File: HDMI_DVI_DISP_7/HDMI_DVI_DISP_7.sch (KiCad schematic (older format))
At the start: 0 parts

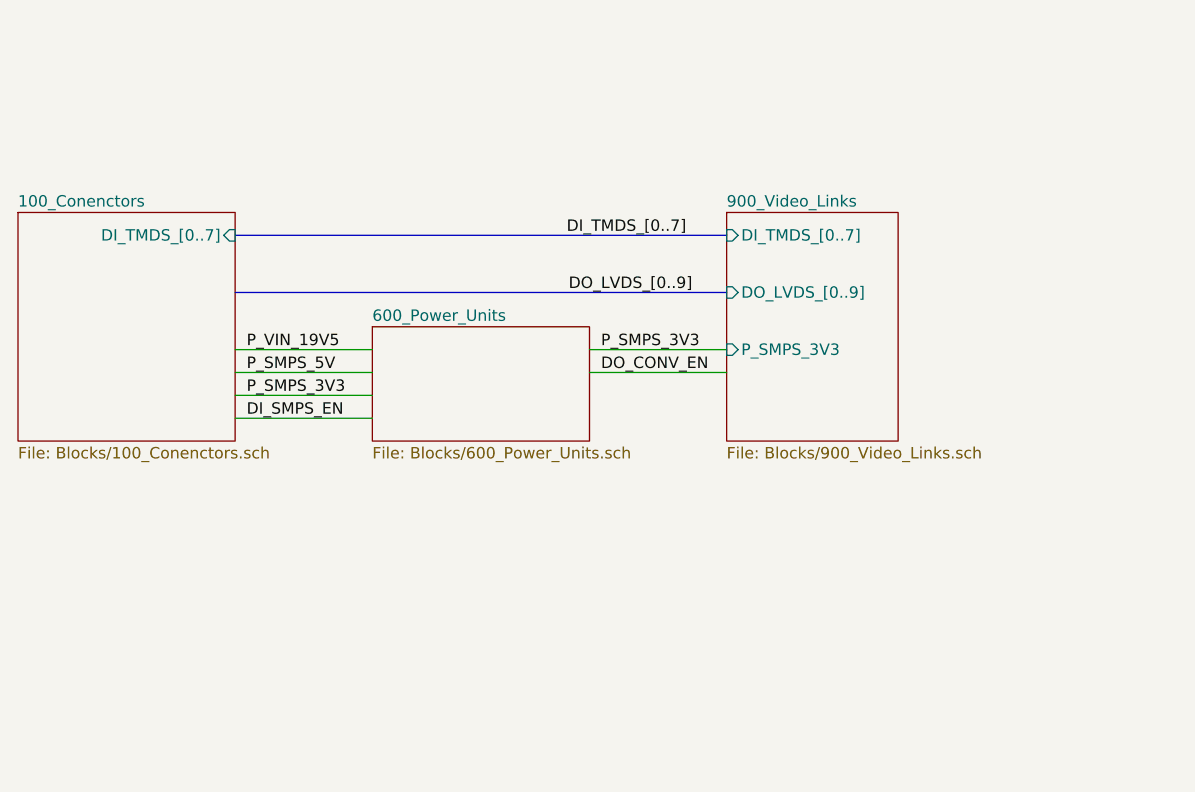
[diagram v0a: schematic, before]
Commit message: The base structure defined for PS
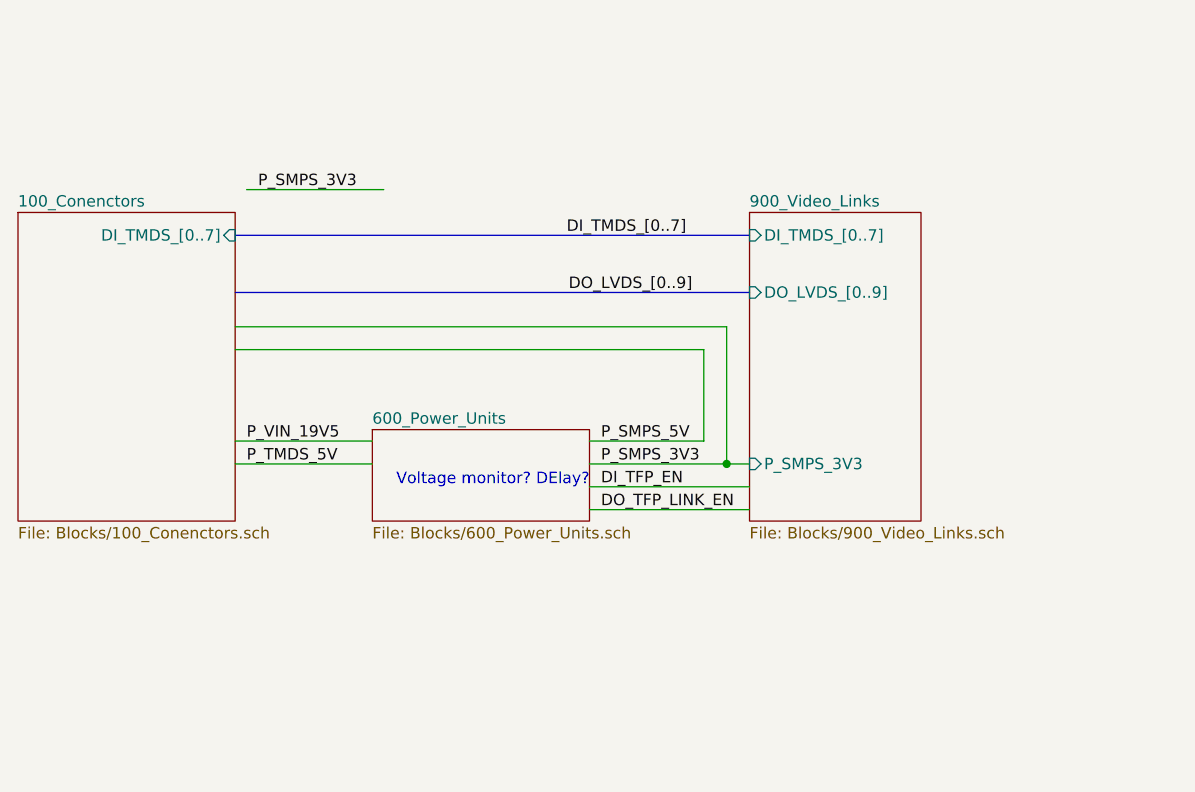
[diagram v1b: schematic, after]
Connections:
- net labels added: DI_TFP_EN, DO_TFP_LINK_EN, P_TMDS_5V
- net labels removed: DI_SMPS_EN, DO_CONV_EN
- wire segments 6 -> 12
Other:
- note added: "Voltage monitor? DElay?"
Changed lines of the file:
@@
 $EndDescr
 $Sheet
-S 3850 2900 950  1000
+S 3850 2900 950  1350
 U 607739A5
 F0 "100_Conenctors" 50
@@
 $EndSheet
 $Sheet
-S 5400 3400 950  500
+S 5400 3850 950  400
 U 60773A19
 F0 "600_Power_Units" 50
@@
 $EndSheet
 $Sheet
-S 6950 2900 750  1000
+S 7050 2900 750  1350
 U 60773BC4
 F0 "900_Video_Links" 50
 F1 "Blocks/900_Video_Links.sch" 50
-F2 "DO_LVDS_[0..9]" I L 6950 3250 50
-F3 "DI_TMDS_[0..7]" I L 6950 3000 50
-F4 "P_SMPS_3V3" I L 6950 3500 50
+F2 "DO_LVDS_[0..9]" I L 7050 3250 50
+F3 "DI_TMDS_[0..7]" I L 7050 3000 50
+F4 "P_SMPS_3V3" I L 7050 4000 50
 $EndSheet
 Text Label 6800 3250 2    50   ~ 0
 DO_LVDS_[0..9]
 Wire Bus Line
-	6950 3000 4800 3000
+	7050 3000 4800 3000
 Text Label 6250 3000 0    50   ~ 0
 DI_TMDS_[0..7]
 Wire Bus Line
-	6950 3250 4800 3250
+	7050 3250 4800 3250
 Wire Wire Line
-	6350 3500 6950 3500
-Text Label 6400 3500 0    50   ~ 0
+	6350 4000 6950 4000
+Text Label 6400 4000 0    50   ~ 0
 P_SMPS_3V3
-Text Label 4850 3500 0    50   ~ 0
+Text Label 4850 3900 0    50   ~ 0
 P_VIN_19V5
 Wire Wire Line
-	4800 3500 5400 3500
-Wire Wire Line
-	4800 3600 5400 3600
-Text Label 4850 3600 0    50   ~ 0
+	4800 3900 5400 3900
+Text Label 6400 3900 0    50   ~ 0
 P_SMPS_5V
-Text Label 4850 3700 0    50   ~ 0
+Text Label 4900 2800 0    50   ~ 0
 P_SMPS_3V3
 Wire Wire Line
-	4800 3700 5400 3700
+	4850 2800 5450 2800
 Wire Wire Line
-	4800 3800 5400 3800
-Text Label 4850 3800 0    50   ~ 0
-DI_SMPS_EN
+	4800 4000 5400 4000
+Text Label 6400 4100 0    50   ~ 0
+DI_TFP_EN
+Text Label 4850 4000 0    50   ~ 0
+P_TMDS_5V
+Text Notes 6350 4100 2    50   ~ 0
+Voltage monitor? DElay?
+Text Label 6400 4200 0    50   ~ 0
+DO_TFP_LINK_EN
 Wire Wire Line
-	6350 3600 6950 3600
-Text Label 6400 3600 0    50   ~ 0
-DO_CONV_EN
+	6950 4000 6950 3400
+Wire Wire Line
+	6950 3400 4800 3400
+Connection ~ 6950 4000
+Wire Wire Line
+	6950 4000 7050 4000
+Wire Wire Line
+	6350 4100 7050 4100
+Wire Wire Line
+	6350 4200 7050 4200
+Wire Wire Line
+	6350 3900 6850 3900
+Wire Wire Line
+	6850 3900 6850 3500
+Wire Wire Line
+	6850 3500 4800 3500
 $EndSCHEMATC

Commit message: Daily job done
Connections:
- net labels added: DO_SYNC_DET
- net labels removed: DI_TFP_EN, DO_TFP_LINK_EN
- wire segments 12 -> 11
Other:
- note removed: "Voltage monitor? DElay?"
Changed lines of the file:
@@
 F0 "100_Conenctors" 50
 F1 "Blocks/100_Conenctors.sch" 50
-F2 "DI_TMDS_[0..7]" I R 4800 3000 50
+F2 "DI_TMDS_[0..7]" O R 4800 3000 50
+F3 "P_TMDS_5V" O R 4800 4000 50
+F4 "EN_MATRIX_EDID" I R 4800 3400 50
+F5 "P_SMPS_3V3" I R 4800 3500 50
+F6 "P_SMPS_5V" I R 4800 3600 50
+F7 "P_VIN_19V5" O R 4800 3900 50
+F8 "DO_LVDS_[0..9]" I R 4800 3250 50
 $EndSheet
 $Sheet
-S 5400 3850 950  400
-U 60773A19
-F0 "600_Power_Units" 50
-F1 "Blocks/600_Power_Units.sch" 50
-$EndSheet
-$Sheet
-S 7050 2900 750  1350
+S 7400 2900 750  1350
 U 60773BC4
 F0 "900_Video_Links" 50
 F1 "Blocks/900_Video_Links.sch" 50
-F2 "DO_LVDS_[0..9]" I L 7050 3250 50
-F3 "DI_TMDS_[0..7]" I L 7050 3000 50
-F4 "P_SMPS_3V3" I L 7050 4000 50
+F2 "DO_LVDS_[0..9]" O L 7400 3250 50
+F3 "DI_TMDS_[0..7]" I L 7400 3000 50
+F4 "P_SMPS_3V3" I L 7400 4000 50
+F5 "DO_SYNC_DET" O L 7400 4100 50
+F6 "DO_LVDS_EDID" O L 7400 3400 50
 $EndSheet
 Text Label 6800 3250 2    50   ~ 0
 DO_LVDS_[0..9]
 Wire Bus Line
-	7050 3000 4800 3000
+	7400 3000 4800 3000
 Text Label 6250 3000 0    50   ~ 0
 DI_TMDS_[0..7]
 Wire Bus Line
-	7050 3250 4800 3250
+	7400 3250 4800 3250
 Wire Wire Line
-	6350 4000 6950 4000
-Text Label 6400 4000 0    50   ~ 0
+	6500 4000 7300 4000
+Text Label 6550 4000 0    50   ~ 0
 P_SMPS_3V3
 Text Label 4850 3900 0    50   ~ 0
@@
 Wire Wire Line
 	4800 3900 5400 3900
-Text Label 6400 3900 0    50   ~ 0
+Text Label 6550 3900 0    50   ~ 0
 P_SMPS_5V
-Text Label 4900 2800 0    50   ~ 0
-P_SMPS_3V3
-Wire Wire Line
-	4850 2800 5450 2800
 Wire Wire Line
 	4800 4000 5400 4000
-Text Label 6400 4100 0    50   ~ 0
-DI_TFP_EN
 Text Label 4850 4000 0    50   ~ 0
 P_TMDS_5V
-Text Notes 6350 4100 2    50   ~ 0
-Voltage monitor? DElay?
-Text Label 6400 4200 0    50   ~ 0
-DO_TFP_LINK_EN
 Wire Wire Line
-	6950 4000 6950 3400
+	7300 4000 7300 3500
 Wire Wire Line
-	6950 3400 4800 3400
-Connection ~ 6950 4000
+	7300 3500 4800 3500
+Connection ~ 7300 4000
 Wire Wire Line
-	6950 4000 7050 4000
+	7300 4000 7400 4000
 Wire Wire Line
-	6350 4100 7050 4100
+	6500 4100 7400 4100
 Wire Wire Line
-	6350 4200 7050 4200
+	7200 3900 7200 3600
 Wire Wire Line
-	6350 3900 6850 3900
+	7200 3600 4800 3600
+$Sheet
+S 5400 3850 1100 400
+U 60773A19
+F0 "600_Power_Units" 50
+F1 "Blocks/600_Power_Units.sch" 50
+F2 "P_SMPS_3V3" O R 6500 4000 50
+F3 "P_SMPS_5V" O R 6500 3900 50
+F4 "P_VIN_19V5" I L 5400 3900 50
+F5 "3V3_EN" I L 5400 4000 50
+F6 "5V_EN" I R 6500 4100 50
+$EndSheet
 Wire Wire Line
-	6850 3900 6850 3500
+	6500 3900 7200 3900
+Text Label 6550 4100 0    50   ~ 0
+DO_SYNC_DET
 Wire Wire Line
-	6850 3500 4800 3500
+	4800 3400 7400 3400
 $EndSCHEMATC

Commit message: PS Layout done
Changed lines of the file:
@@
 $EndDescr
 $Sheet
-S 3850 2900 950  1350
+S 3850 2150 950  3100
 U 607739A5
 F0 "100_Conenctors" 50
 F1 "Blocks/100_Conenctors.sch" 50
-F2 "DI_TMDS_[0..7]" O R 4800 3000 50
-F3 "P_TMDS_5V" O R 4800 4000 50
-F4 "EN_MATRIX_EDID" I R 4800 3400 50
-F5 "P_SMPS_3V3" I R 4800 3500 50
-F6 "P_SMPS_5V" I R 4800 3600 50
-F7 "P_VIN_19V5" O R 4800 3900 50
-F8 "DO_LVDS_[0..9]" I R 4800 3250 50
+F2 "P_TMDS_5V" O R 4800 5000 50
+F3 "EN_MATRIX_EDID" I R 4800 4400 50
+F4 "P_SMPS_3V3" I R 4800 4500 50
+F5 "P_SMPS_5V" I R 4800 4600 50
+F6 "P_VIN_19V5" O R 4800 4900 50
+F7 "DI_TMDS_CLK-" O R 4800 2200 50
+F8 "DI_TMDS_CLK+" O R 4800 2300 50
+F9 "DI_TMDS_D0-" O R 4800 2400 50
+F10 "DI_TMDS_D0+" O R 4800 2500 50
+F11 "DI_TMDS_D1-" O R 4800 2600 50
+F12 "DI_TMDS_D1+" O R 4800 2700 50
+F13 "DI_TMDS_D2-" O R 4800 2800 50
+F14 "DI_TMDS_D2+" O R 4800 2900 50
+F15 "DO_LVDS_D0+" I R 4800 3200 50
+F16 "DO_LVDS_D1+" I R 4800 3400 50
+F17 "DO_LVDS_D1-" I R 4800 3300 50
+F18 "DO_LVDS_D2+" I R 4800 3600 50
+F19 "DO_LVDS_D3-" I R 4800 3700 50
+F20 "DO_LVDS_D2-" I R 4800 3500 50
+F21 "DO_LVDS_D3+" I R 4800 3800 50
+F22 "DO_LVDS_CLK-" I R 4800 3900 50
+F23 "DO_LVDS_CLK+" I R 4800 4000 50
+F24 "DO_LVDS_D0-" I R 4800 3100 50
 $EndSheet
 $Sheet
-S 7400 2900 750  1350
+S 7400 2150 850  3100
 U 60773BC4
 F0 "900_Video_Links" 50
 F1 "Blocks/900_Video_Links.sch" 50
-F2 "DO_LVDS_[0..9]" O L 7400 3250 50
-F3 "DI_TMDS_[0..7]" I L 7400 3000 50
-F4 "P_SMPS_3V3" I L 7400 4000 50
-F5 "DO_SYNC_DET" O L 7400 4100 50
-F6 "DO_LVDS_EDID" O L 7400 3400 50
+F2 "P_SMPS_3V3" I L 7400 5000 50
+F3 "DO_SYNC_DET" O L 7400 5100 50
+F4 "DO_LVDS_EDID" O L 7400 4400 50
+F5 "DI_TMDS_CLK-" I L 7400 2200 50
+F6 "DI_TMDS_CLK+" I L 7400 2300 50
+F7 "DI_TMDS_D0-" I L 7400 2400 50
+F8 "DI_TMDS_D0+" I L 7400 2500 50
+F9 "DI_TMDS_D1-" I L 7400 2600 50
+F10 "DI_TMDS_D1+" I L 7400 2700 50
+F11 "DI_TMDS_D2-" I L 7400 2800 50
+F12 "DI_TMDS_D2+" I L 7400 2900 50
+F13 "DO_LVDS_D0-" O L 7400 3100 50
+F14 "DO_LVDS_D0+" O L 7400 3200 50
+F15 "DO_LVDS_D1+" O L 7400 3400 50
+F16 "DO_LVDS_D1-" O L 7400 3300 50
+F17 "DO_LVDS_D2+" O L 7400 3600 50
+F18 "DO_LVDS_D3-" O L 7400 3700 50
+F19 "DO_LVDS_D2-" O L 7400 3500 50
+F20 "DO_LVDS_D3+" O L 7400 3800 50
+F21 "DO_LVDS_CLK-" O L 7400 3900 50
+F22 "DO_LVDS_CLK+" O L 7400 4000 50
 $EndSheet
-Text Label 6800 3250 2    50   ~ 0
-DO_LVDS_[0..9]
-Wire Bus Line
-	7400 3000 4800 3000
-Text Label 6250 3000 0    50   ~ 0
-DI_TMDS_[0..7]
-Wire Bus Line
-	7400 3250 4800 3250
 Wire Wire Line
-	6500 4000 7300 4000
-Text Label 6550 4000 0    50   ~ 0
+	6500 5000 7300 5000
+Text Label 6550 5000 0    50   ~ 0
 P_SMPS_3V3
-Text Label 4850 3900 0    50   ~ 0
+Text Label 4850 4900 0    50   ~ 0
 P_VIN_19V5
 Wire Wire Line
-	4800 3900 5400 3900
-Text Label 6550 3900 0    50   ~ 0
+	4800 4900 5400 4900
+Text Label 6550 4900 0    50   ~ 0
 P_SMPS_5V
 Wire Wire Line
-	4800 4000 5400 4000
-Text Label 4850 4000 0    50   ~ 0
+	4800 5000 5400 5000
+Text Label 4850 5000 0    50   ~ 0
 P_TMDS_5V
 Wire Wire Line
-	7300 4000 7300 3500
+	7300 5000 7300 4500
 Wire Wire Line
-	7300 3500 4800 3500
-Connection ~ 7300 4000
+	7300 4500 4800 4500
+Connection ~ 7300 5000
 Wire Wire Line
-	7300 4000 7400 4000
+	7300 5000 7400 5000
 Wire Wire Line
-	6500 4100 7400 4100
+	6500 5100 7400 5100
 Wire Wire Line
-	7200 3900 7200 3600
+	7200 4900 7200 4600
 Wire Wire Line
-	7200 3600 4800 3600
+	7200 4600 4800 4600
 $Sheet
-S 5400 3850 1100 400
+S 5400 4850 1100 400
 U 60773A19
 F0 "600_Power_Units" 50
 F1 "Blocks/600_Power_Units.sch" 50
-F2 "P_SMPS_3V3" O R 6500 4000 50
-F3 "P_SMPS_5V" O R 6500 3900 50
-F4 "P_VIN_19V5" I L 5400 3900 50
-F5 "3V3_EN" I L 5400 4000 50
-F6 "5V_EN" I R 6500 4100 50
+F2 "P_SMPS_3V3" O R 6500 5000 50
+F3 "P_SMPS_5V" O R 6500 4900 50
+F4 "P_VIN_19V5" I L 5400 4900 50
+F5 "3V3_EN" I L 5400 5000 50
+F6 "5V_EN" I R 6500 5100 50
 $EndSheet
 Wire Wire Line
-	6500 3900 7200 3900
-Text Label 6550 4100 0    50   ~ 0
+	6500 4900 7200 4900
+Text Label 6550 5100 0    50   ~ 0
 DO_SYNC_DET
 Wire Wire Line
-	4800 3400 7400 3400
+	4800 4400 7400 4400
+Wire Wire Line
+	4800 2200 7400 2200
+Wire Wire Line
+	4800 2300 7400 2300
+Wire Wire Line
+	4800 2400 7400 2400
+Wire Wire Line
+	4800 2500 7400 2500
+Wire Wire Line
+	4800 2600 7400 2600
+Wire Wire Line
+	4800 2700 7400 2700
+Wire Wire Line
+	4800 2800 7400 2800
+Wire Wire Line
+	4800 2900 7400 2900
+Wire Wire Line
+	7400 3100 4800 3100
+Wire Wire Line
+	7400 3200 4800 3200
+Wire Wire Line
+	7400 3300 4800 3300
+Wire Wire Line
+	7400 3400 4800 3400
+Wire Wire Line
+	7400 3500 4800 3500
+Wire Wire Line
+	7400 3600 4800 3600
+Wire Wire Line
+	7400 3700 4800 3700
+Wire Wire Line
+	7400 3800 4800 3800
+Wire Wire Line
+	7400 3900 4800 3900
+Wire Wire Line
+	7400 4000 4800 4000
 $EndSCHEMATC
